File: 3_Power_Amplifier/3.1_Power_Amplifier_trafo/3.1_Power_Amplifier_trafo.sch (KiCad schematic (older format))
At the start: 11 parts, among them P1 IN_SWITCHEO, P2 OUT_CON_CAP, P3 OUT_SIN_CAP, P4 IN_FUENTE_CONM, T1 TRANSFO-SO12

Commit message: AMPLIFICADOR DE POTENCIA_2 PCB_UNO
CON ISLETAS Y DISIPADORES VERTICALES
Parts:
- removed P4: IN_FUENTE_CONM, Sockets_MOLEX_KK-System:Socket_MOLEX-KK-RM3-96mm_Lock_4pin_straight, symbol IN_FUENTE_CONM
- added P10, P4: TIERRA_POT, Sockets_MOLEX_KK-System:Socket_MOLEX-KK-RM3-96mm_Lock_2pin_straight, symbol TIERRA_POT
- added P5, P6, P7, P8: ISLETA, libreria_Power_Amplifier_huellas:Pad_Via_5.1mm_TOR, symbol ISLETA
- added P9: IN_FUENTE_CONM, Sockets_MOLEX_KK-System:Socket_MOLEX-KK-RM3-96mm_Lock_2pin_straight, symbol IN_FUENTE_CONM
- P1: footprint Sockets_MOLEX_KK-System:Socket_MOLEX-KK-RM3-96mm_Lock_4pin_straight -> Sockets_MOLEX_KK-System:Socket_MOLEX-KK-RM3-96mm_Lock_2pin_straight
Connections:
- no-connect marks 0 -> 4
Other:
- note added: "ISLETAS"
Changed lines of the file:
@@
 	1    0    0    -1
 $EndComp
-$Comp
-L IN_FUENTE_CONM P4
-U 1 1 59CFA514
-P 1200 4000
-F 0 "P4" H 1200 4250 50  0000 C CNN
-F 1 "IN_FUENTE_CONM" V 1300 4000 50  0000 C CNN
-F 2 "Sockets_MOLEX_KK-System:Socket_MOLEX-KK-RM3-96mm_Lock_4pin_straight" H 1100 4150 50  0001 C CNN
-F 3 "" H 1200 4000 50  0000 C CNN
-	1    1200 4000
-	-1   0    0    1
-$EndComp
 Wire Notes Line
 	750  1100 11000 1100
@@
 	11000 4500 750  4500
 Wire Notes Line
-	750  4500 750  1100
+	750  1100 750  5600
 Text Notes 1050 1300 0    79   ~ 16
 CONECTORES
-$Comp
-L IN_SWITCHEO P1
-U 1 1 59CFAC64
-P 1200 1950
-F 0 "P1" H 1200 2200 50  0000 C CNN
-F 1 "IN_SWITCHEO" V 1300 1950 50  0000 C CNN
-F 2 "Sockets_MOLEX_KK-System:Socket_MOLEX-KK-RM3-96mm_Lock_4pin_straight" H 1100 2100 50  0001 C CNN
-F 3 "" H 1200 1950 50  0000 C CNN
-	1    1200 1950
-	-1   0    0    1
-$EndComp
 Text Notes 4100 1550 0    79   ~ 16
 ARREGLO DE CAPACITORES \nTANQUE LC
@@
 	6900 1100 6900 6100
 Wire Notes Line
-	3050 4500 3050 1100
+	3050 1100 3050 5600
 Text Label 7800 3150 0    79   ~ 16
 VDD
@@
 	-1   0    0    1
 $EndComp
+$Comp
+L ISLETA P5
+U 1 1 59D07AFC
+P 1300 4850
+F 0 "P5" H 1300 4950 50  0000 C CNN
+F 1 "ISLETA" V 1400 4850 50  0000 C CNN
+F 2 "libreria_Power_Amplifier_huellas:Pad_Via_5.1mm_TOR" H 1200 4850 50  0001 C CNN
+F 3 "" H 1300 4950 50  0000 C CNN
+	1    1300 4850
+	-1   0    0    1
+$EndComp
+$Comp
+L ISLETA P6
+U 1 1 59D07C9B
+P 1300 5250
+F 0 "P6" H 1300 5350 50  0000 C CNN
+F 1 "ISLETA" V 1400 5250 50  0000 C CNN
+F 2 "libreria_Power_Amplifier_huellas:Pad_Via_5.1mm_TOR" H 1200 5250 50  0001 C CNN
+F 3 "" H 1300 5350 50  0000 C CNN
+	1    1300 5250
+	-1   0    0    1
+$EndComp
+$Comp
+L ISLETA P7
+U 1 1 59D07CDC
+P 2300 4850
+F 0 "P7" H 2300 4950 50  0000 C CNN
+F 1 "ISLETA" V 2400 4850 50  0000 C CNN
+F 2 "libreria_Power_Amplifier_huellas:Pad_Via_5.1mm_TOR" H 2200 4850 50  0001 C CNN
+F 3 "" H 2300 4950 50  0000 C CNN
+	1    2300 4850
+	-1   0    0    1
+$EndComp
+$Comp
+L ISLETA P8
+U 1 1 59D07D6C
+P 2300 5250
+F 0 "P8" H 2300 5350 50  0000 C CNN
+F 1 "ISLETA" V 2400 5250 50  0000 C CNN
+F 2 "libreria_Power_Amplifier_huellas:Pad_Via_5.1mm_TOR" H 2200 5250 50  0001 C CNN
+F 3 "" H 2300 5350 50  0000 C CNN
+	1    2300 5250
+	-1   0    0    1
+$EndComp
+NoConn ~ 2500 4850
+NoConn ~ 2500 5250
+NoConn ~ 1500 5250
+NoConn ~ 1500 4850
+Wire Notes Line
+	3050 5600 750  5600
+Text Notes 1600 4650 0    79   ~ 16
+ISLETAS
+$Comp
+L IN_SWITCHEO P1
+U 1 1 59D04926
+P 1200 1850
+F 0 "P1" H 1300 1850 50  0000 C CNN
+F 1 "IN_SWITCHEO" H 1200 1700 50  0000 C CNN
+F 2 "Sockets_MOLEX_KK-System:Socket_MOLEX-KK-RM3-96mm_Lock_2pin_straight" H 1100 1900 50  0001 C CNN
+F 3 "" H 1200 1850 50  0000 C CNN
+	1    1200 1850
+	-1   0    0    1
+$EndComp
+$Comp
+L TIERRA_POT P4
+U 1 1 59D04A46
+P 1200 2050
+F 0 "P4" H 1300 2050 50  0000 C CNN
+F 1 "TIERRA_POT" H 1200 2200 50  0000 C CNN
+F 2 "Sockets_MOLEX_KK-System:Socket_MOLEX-KK-RM3-96mm_Lock_2pin_straight" H 1100 2100 50  0001 C CNN
+F 3 "" H 1200 2050 50  0000 C CNN
+	1    1200 2050
+	-1   0    0    1
+$EndComp
+$Comp
+L IN_FUENTE_CONM P9
+U 1 1 59D05006
+P 1200 3900
+F 0 "P9" H 1300 3900 50  0000 C CNN
+F 1 "IN_FUENTE_CONM" H 1200 3750 50  0000 C CNN
+F 2 "Sockets_MOLEX_KK-System:Socket_MOLEX-KK-RM3-96mm_Lock_2pin_straight" H 1100 3950 50  0001 C CNN
+F 3 "" H 1200 3900 50  0000 C CNN
+	1    1200 3900
+	-1   0    0    1
+$EndComp
+$Comp
+L TIERRA_POT P10
+U 1 1 59D050DC
+P 1200 4100
+F 0 "P10" H 1300 4100 50  0000 C CNN
+F 1 "TIERRA_POT" H 1200 4250 50  0000 C CNN
+F 2 "Sockets_MOLEX_KK-System:Socket_MOLEX-KK-RM3-96mm_Lock_2pin_straight" H 1100 4150 50  0001 C CNN
+F 3 "" H 1200 4100 50  0000 C CNN
+	1    1200 4100
+	-1   0    0    1
+$EndComp

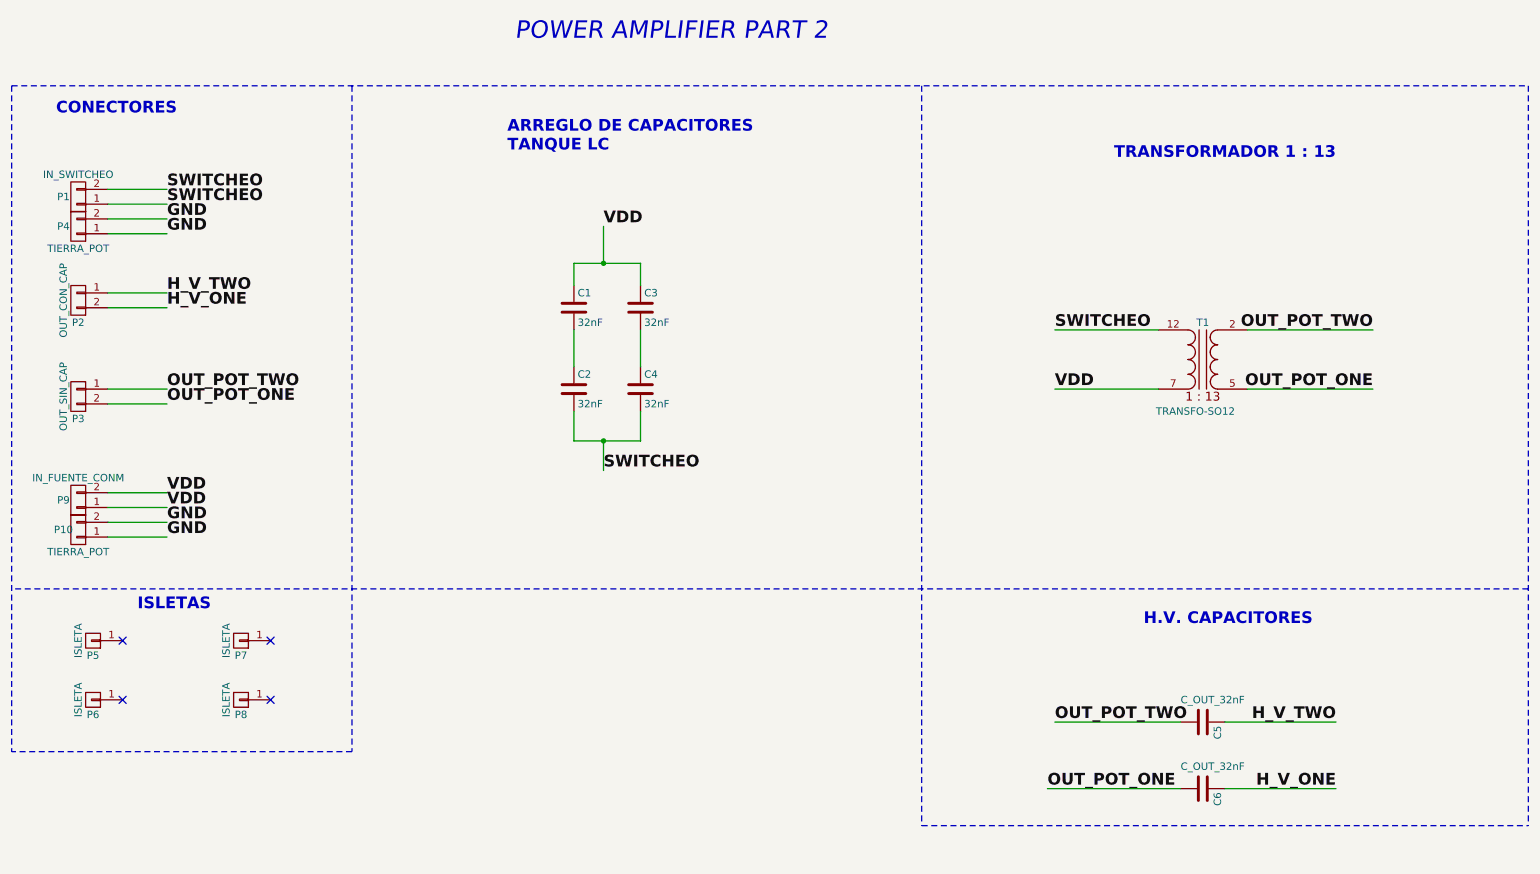
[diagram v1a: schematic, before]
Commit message: AMPLIFICADOR DE POTENCIAS_2 PCB_V2
modificaciones a la pcb del trafo
falta arreglos a la pcb de los mosfet
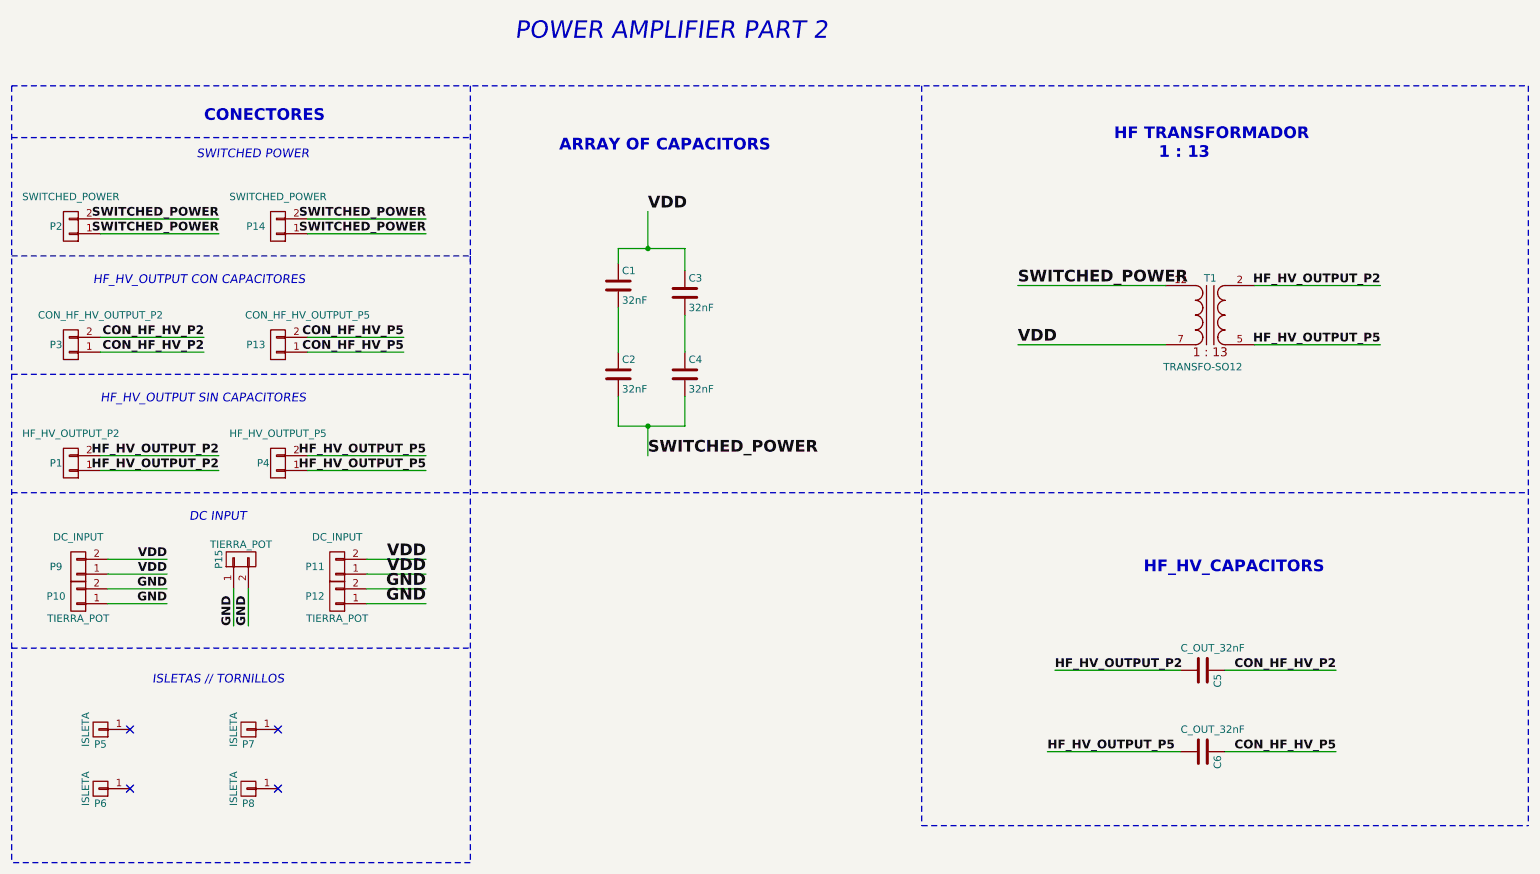
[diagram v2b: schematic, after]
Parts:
- removed P1: IN_SWITCHEO, Sockets_MOLEX_KK-System:Socket_MOLEX-KK-RM3-96mm_Lock_2pin_straight, symbol IN_SWITCHEO
- removed P2: OUT_CON_CAP, libreria_Power_Amplifier_huellas:Socket_MOLEX-KK-RM3-96mm_Lock_2pin_straight, symbol OUT_CON_CAP
- removed P3: OUT_SIN_CAP, libreria_Power_Amplifier_huellas:Socket_MOLEX-KK-RM3-96mm_Lock_2pin_straight, symbol OUT_SIN_CAP
- removed P4: TIERRA_POT, Sockets_MOLEX_KK-System:Socket_MOLEX-KK-RM3-96mm_Lock_2pin_straight, symbol TIERRA_POT
- removed P9: IN_FUENTE_CONM, Sockets_MOLEX_KK-System:Socket_MOLEX-KK-RM3-96mm_Lock_2pin_straight, symbol IN_FUENTE_CONM
- added P1: HF_HV_OUTPUT_P2, Sockets_MOLEX_KK-System:Socket_MOLEX-KK-RM3-96mm_Lock_2pin_straight, symbol HF_HV_OUTPUT_P2
- added P11, P9: DC_INPUT, Sockets_MOLEX_KK-System:Socket_MOLEX-KK-RM3-96mm_Lock_2pin_straight, symbol DC_INPUT
- added P12, P15: TIERRA_POT, Sockets_MOLEX_KK-System:Socket_MOLEX-KK-RM3-96mm_Lock_2pin_straight, symbol TIERRA_POT
- added P13: CON_HF_HV_OUTPUT_P5, Sockets_MOLEX_KK-System:Socket_MOLEX-KK-RM3-96mm_Lock_2pin_straight, symbol CON_HF_HV_OUTPUT_P5
- added P14, P2: SWITCHED_POWER, Sockets_MOLEX_KK-System:Socket_MOLEX-KK-RM3-96mm_Lock_2pin_straight, symbol SWITCHED_POWER
- added P3: CON_HF_HV_OUTPUT_P2, Sockets_MOLEX_KK-System:Socket_MOLEX-KK-RM3-96mm_Lock_2pin_straight, symbol CON_HF_HV_OUTPUT_P2
- added P4: HF_HV_OUTPUT_P5, Sockets_MOLEX_KK-System:Socket_MOLEX-KK-RM3-96mm_Lock_2pin_straight, symbol HF_HV_OUTPUT_P5
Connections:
- net GND: now also P12.1 (P1), P12.2 (P2), P15.1 (P1), P15.2 (P2)
- net VDD: now also P11.1 (P1), P11.2 (P2), P9.1 (P1), P9.2 (P2)
- net H_V_ONE renamed CON_HF_HV_P5
- net CON_HF_HV_P5: now also P13.1 (P1), P13.2 (P2)
- net H_V_TWO renamed CON_HF_HV_P2
- net CON_HF_HV_P2: now also P3.1 (P1), P3.2 (P2)
- net OUT_POT_ONE renamed HF_HV_OUTPUT_P5
- net HF_HV_OUTPUT_P5: now also P4.1 (P1), P4.2 (P2)
- net OUT_POT_TWO renamed HF_HV_OUTPUT_P2
- net HF_HV_OUTPUT_P2: now also P1.1 (P1), P1.2 (P2)
- net SWITCHEO renamed SWITCHED_POWER
- net SWITCHED_POWER: now also P14.1 (P1), P14.2 (P2), P2.1 (P1), P2.2 (P2)
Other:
- note added: "ARRAY OF CAPACITORS \n"
- note added: "DC INPUT"
- note added: "HF TRANSFORMADOR \n 1 : 13"
- note added: "HF_HV_CAPACITORS"
- note added: "HF_HV_OUTPUT CON CAPACITORES"
- note added: "HF_HV_OUTPUT SIN CAPACITORES"
- note added: "ISLETAS // TORNILLOS\n"
- note added: "SWITCHED POWER"
- note removed: "ARREGLO DE CAPACITORES \nTANQUE LC"
- note removed: "H.V. CAPACITORES"
- note removed: "ISLETAS"
- note removed: "TRANSFORMADOR 1 : 13"
- moved on the sheet: C1, C2, C3, C4, C5, C6, P10, P5, P6, P7, P8, T1

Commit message: GENERADOR V11
TRAZADO DE PISTAS Y VIAS
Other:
- note added: "POWER AMPLIFIER _ 2"
- note removed: "POWER AMPLIFIER PART 2"
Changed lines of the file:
@@
 	6900 6100 11000 6100
 Text Notes 4150 800  0    118  Italic 0
-POWER AMPLIFIER PART 2
+POWER AMPLIFIER _ 2
 Text Notes 8400 4400 0    79   ~ 16
 HF_HV_CAPACITORS
